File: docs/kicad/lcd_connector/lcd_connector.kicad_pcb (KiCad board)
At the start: 2 copper layers, 17.8 x 38.1 mm, 19 parts, among them J1 5V, J2 T_CS, J3 CLK, J4 MISO, J5 DC, J6 CS, J7 MOSI, J8 GND, M1 TFT_ILI9341

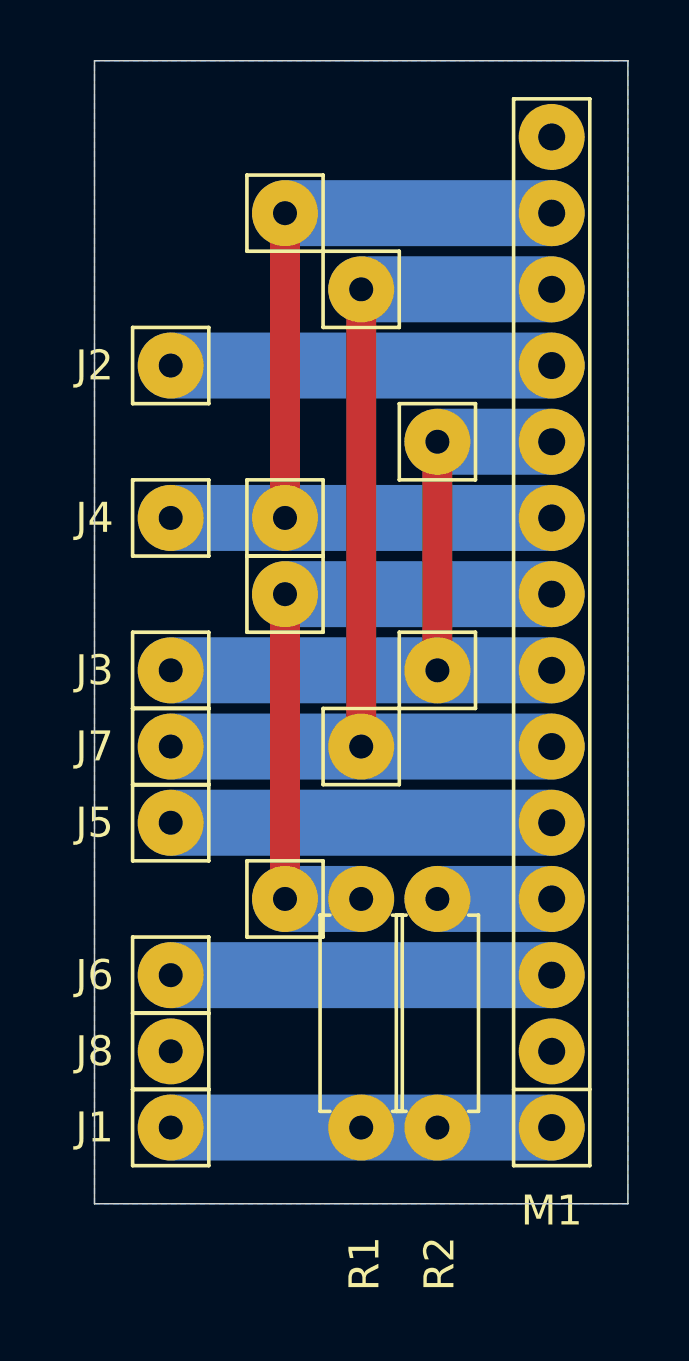
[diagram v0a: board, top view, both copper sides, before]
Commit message: added important 220 ohm resistor with MISO going FIRST to Touch after TE3 testing
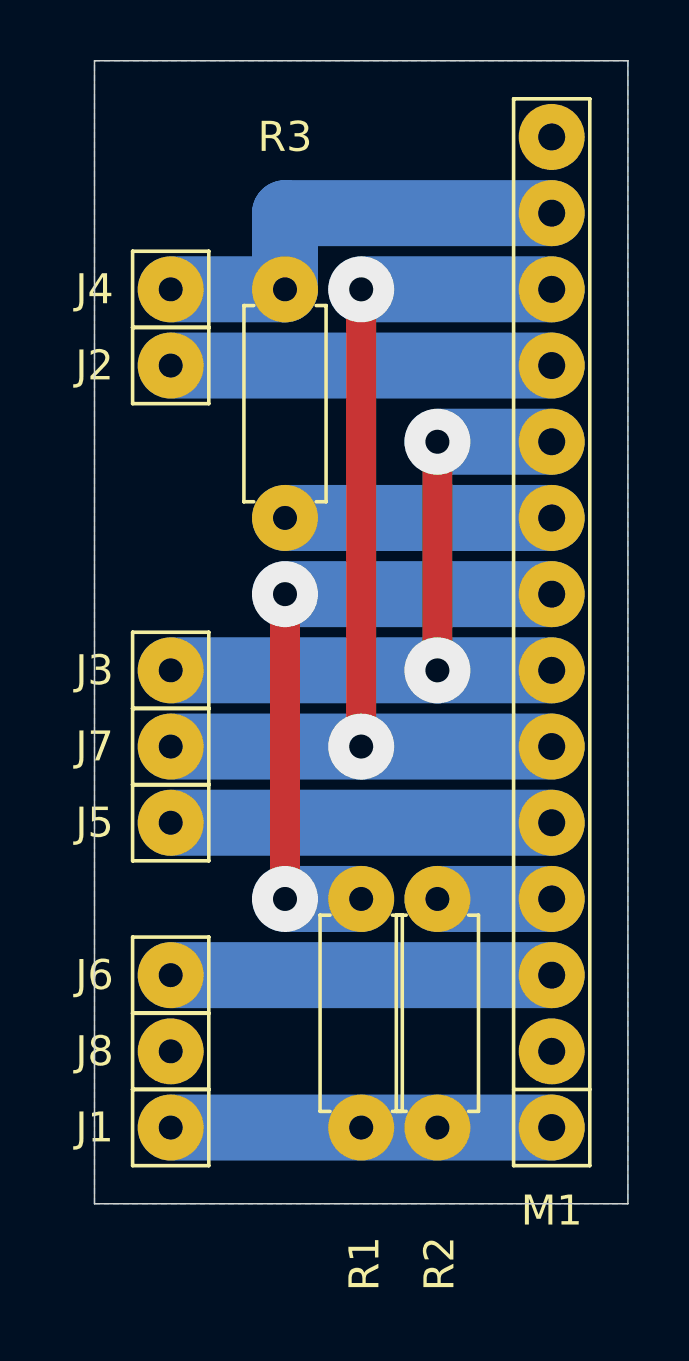
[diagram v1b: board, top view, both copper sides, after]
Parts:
- removed V1, V2, V3, V5, V6, V7, V8, V9: Conn_01x01, cnc3018-PCB:my1pin
- added R3: 220, 0_my_footprints:myResistor, F.Cu at (6.35, -30.5)
- M1: value TFT_ILI9341 -> TFT_ILI9488
- moved J4 7.62 mm to (2.54, -30.5)
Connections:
- M1 pad 9: Net-(J4-Pad1) -> Net-(M1-Pad9)
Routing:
- net Net-(J4-Pad1): track 31.8 -> 15.2 mm
- net Net-(M1-Pad9): track 0.00 -> 8.89 mm
- net Net-(J3-Pad1): vias 0 -> 2
- net Net-(M1-Pad8): vias 0 -> 2
- net Net-(J7-Pad1): vias 0 -> 2
